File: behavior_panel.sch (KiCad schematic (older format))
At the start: 32 parts, among them J1 Conn_01x16, Q1 Q_NPN_BEC, Q3 N-channel MOSFET, U1 LM2902, U2 LM317_3PinPackage, U3 SFH617A-1X007T

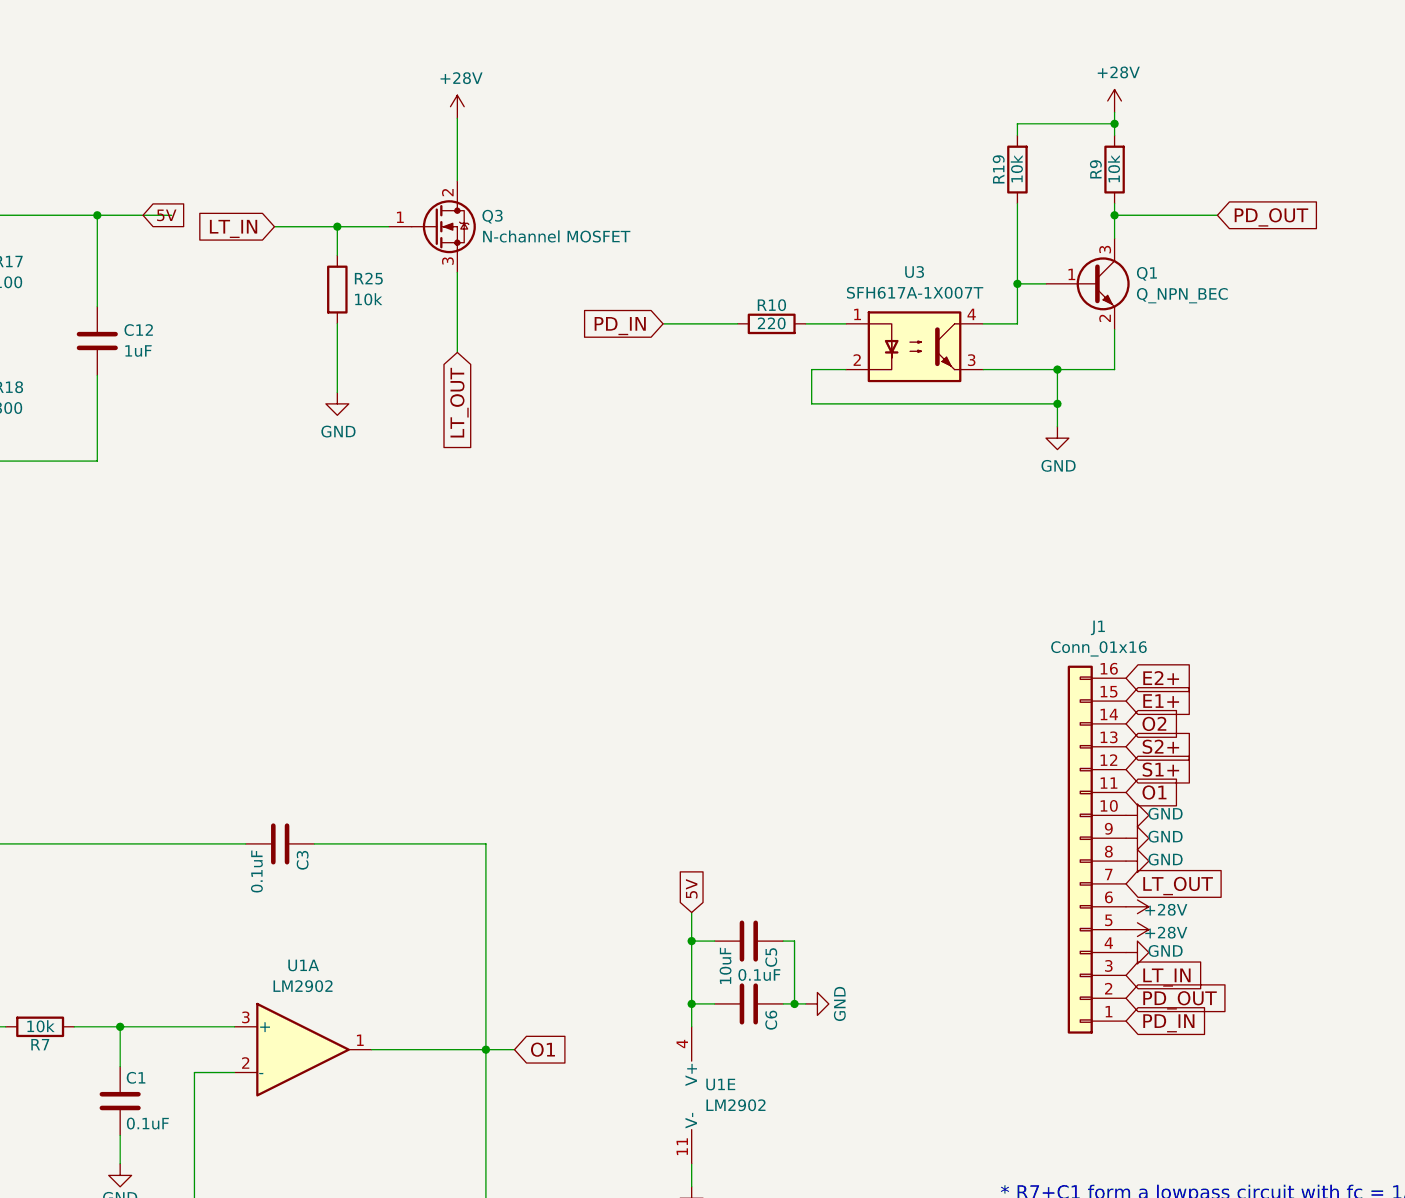
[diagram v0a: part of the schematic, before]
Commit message: Fix bug in MOSFET light control
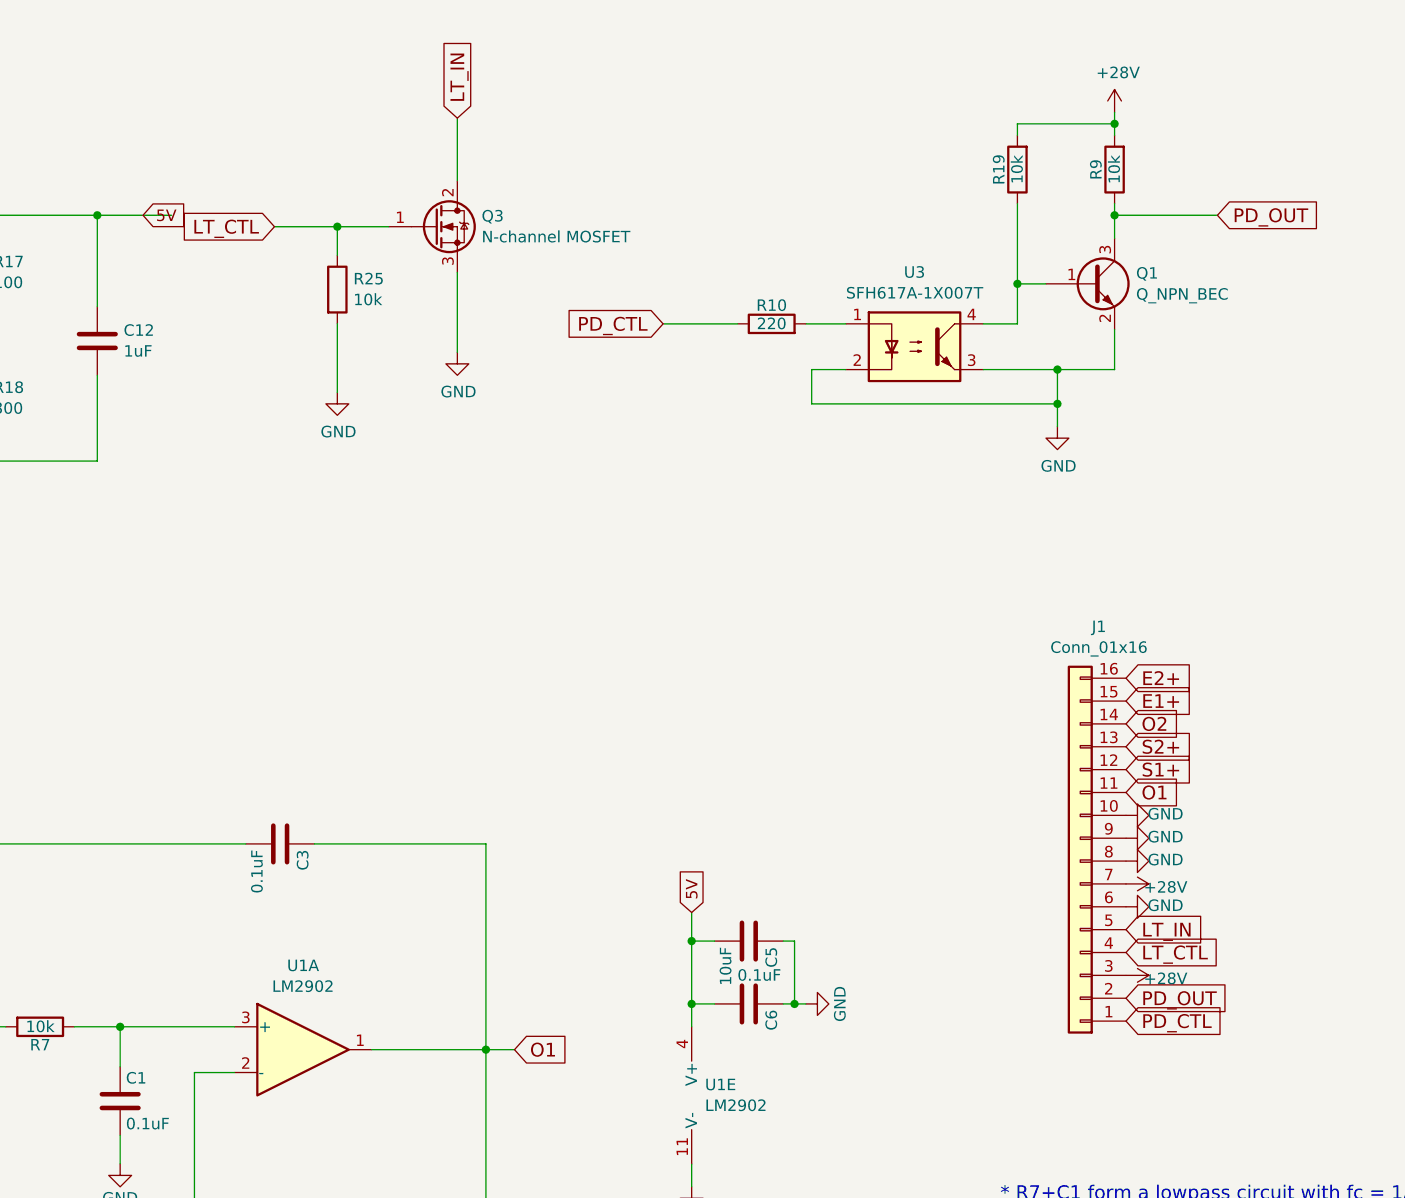
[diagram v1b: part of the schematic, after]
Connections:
- net +28V: now also J1.3 (Pin_3), J1.7 (Pin_7); no longer J1.5 (Pin_5), J1.6 (Pin_6), Q3.2 (D)
- net GND: now also J1.6 (Pin_6), Q3.3 (S); no longer J1.4 (Pin_4)
- net LT_IN: now also J1.5 (Pin_5), Q3.2 (D); no longer J1.3 (Pin_3), Q3.1 (G), R25.1
- removed net LT_OUT: J1.7 (Pin_7), Q3.3 (S)
- net PD_IN renamed PD_CTL
- new net LT_CTL: J1.4 (Pin_4), Q3.1 (G), R25.1
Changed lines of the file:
@@
 	7350 1575 7225 1575
-$Comp
-L power:+28V #PWR03
-U 1 1 5E2C9436
-P 4775 850
-F 0 "#PWR03" H 4775 700 50  0001 C CNN
-F 1 "+28V" H 4790 1023 50  0000 C CNN
-F 2 "" H 5025 900 50  0001 C CNN
-F 3 "" H 5025 900 50  0001 C CNN
-	1    4775 850
-	1    0    0    -1
-$EndComp
 $Comp
 L power:GND #PWR02
@@
 	6475 1750 6300 1750
 Text GLabel 5675 1750 0    60   Input ~ 0
-PD_IN
+PD_CTL
 Wire Wire Line
 	5675 1750 6000 1750
@@
 	6250 4725 6300 4725
 Text GLabel 3975 1325 0    60   Input ~ 0
+LT_CTL
+Text GLabel 4775 850  1    60   Input ~ 0
 LT_IN
-Text GLabel 4775 1875 3    60   Input ~ 0
-LT_OUT
 Wire Wire Line
 	4250 1750 4250 2050
 Wire Wire Line
 	1675 1125 1675 2350
-$Comp
-L power:+28V #PWR06
-U 1 1 5E2D5F4C
-P 7700 4400
-F 0 "#PWR06" H 7700 4250 50  0001 C CNN
-F 1 "+28V" V 7715 4573 50  0000 C CNN
-F 2 "" H 7950 4450 50  0001 C CNN
-F 3 "" H 7950 4450 50  0001 C CNN
-	1    7700 4400
-	0    1    1    0
-$EndComp
 $Comp
 L power:+28V #PWR07
 U 1 1 5E2D81EC
-P 7700 4300
-F 0 "#PWR07" H 7700 4150 50  0001 C CNN
-F 1 "+28V" V 7715 4473 50  0000 C CNN
-F 2 "" H 7950 4350 50  0001 C CNN
-F 3 "" H 7950 4350 50  0001 C CNN
-	1    7700 4300
+P 7700 4200
+F 0 "#PWR07" H 7700 4050 50  0001 C CNN
+F 1 "+28V" V 7715 4373 50  0000 C CNN
+F 2 "" H 7950 4250 50  0001 C CNN
+F 3 "" H 7950 4250 50  0001 C CNN
+	1    7700 4200
 	0    1    1    0
 $EndComp
@@
 L power:GND #PWR08
 U 1 1 5E2D8C1D
-P 7700 4500
-F 0 "#PWR08" H 7700 4250 50  0001 C CNN
-F 1 "GND" V 7705 4327 50  0000 C CNN
-F 2 "" H 7700 4500 50  0001 C CNN
-F 3 "" H 7700 4500 50  0001 C CNN
-	1    7700 4500
+P 7700 4300
+F 0 "#PWR08" H 7700 4050 50  0001 C CNN
+F 1 "GND" V 7705 4127 50  0000 C CNN
+F 2 "" H 7700 4300 50  0001 C CNN
+F 3 "" H 7700 4300 50  0001 C CNN
+	1    7700 4300
 	0    -1   -1   0
 $EndComp
 Text GLabel 7700 4800 2    60   Input ~ 0
-PD_IN
+PD_CTL
 Text GLabel 7700 4700 2    60   Input ~ 0
 PD_OUT
@@
 	-1   0    0    1
 $EndComp
-Text GLabel 7700 4200 2    60   Input ~ 0
-LT_OUT
-Text GLabel 7700 4600 2    60   Input ~ 0
+Text GLabel 7700 4400 2    60   Input ~ 0
 LT_IN
+Text GLabel 7700 4500 2    60   Input ~ 0
+LT_CTL
+$Comp
+L power:GND #PWR0101
+U 1 1 5E4675D1
+P 4775 1875
+F 0 "#PWR0101" H 4775 1625 50  0001 C CNN
+F 1 "GND" H 4780 1702 50  0000 C CNN
+F 2 "" H 4775 1875 50  0001 C CNN
+F 3 "" H 4775 1875 50  0001 C CNN
+	1    4775 1875
+	1    0    0    -1
+$EndComp
+$Comp
+L power:+28V #PWR06
+U 1 1 5E2D5F4C
+P 7700 4600
+F 0 "#PWR06" H 7700 4450 50  0001 C CNN
+F 1 "+28V" V 7715 4773 50  0000 C CNN
+F 2 "" H 7950 4650 50  0001 C CNN
+F 3 "" H 7950 4650 50  0001 C CNN
+	1    7700 4600
+	0    1    1    0
+$EndComp
 $EndSCHEMATC
